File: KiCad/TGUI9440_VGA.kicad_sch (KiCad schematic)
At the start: 20 parts, among them U6 TGUI9440

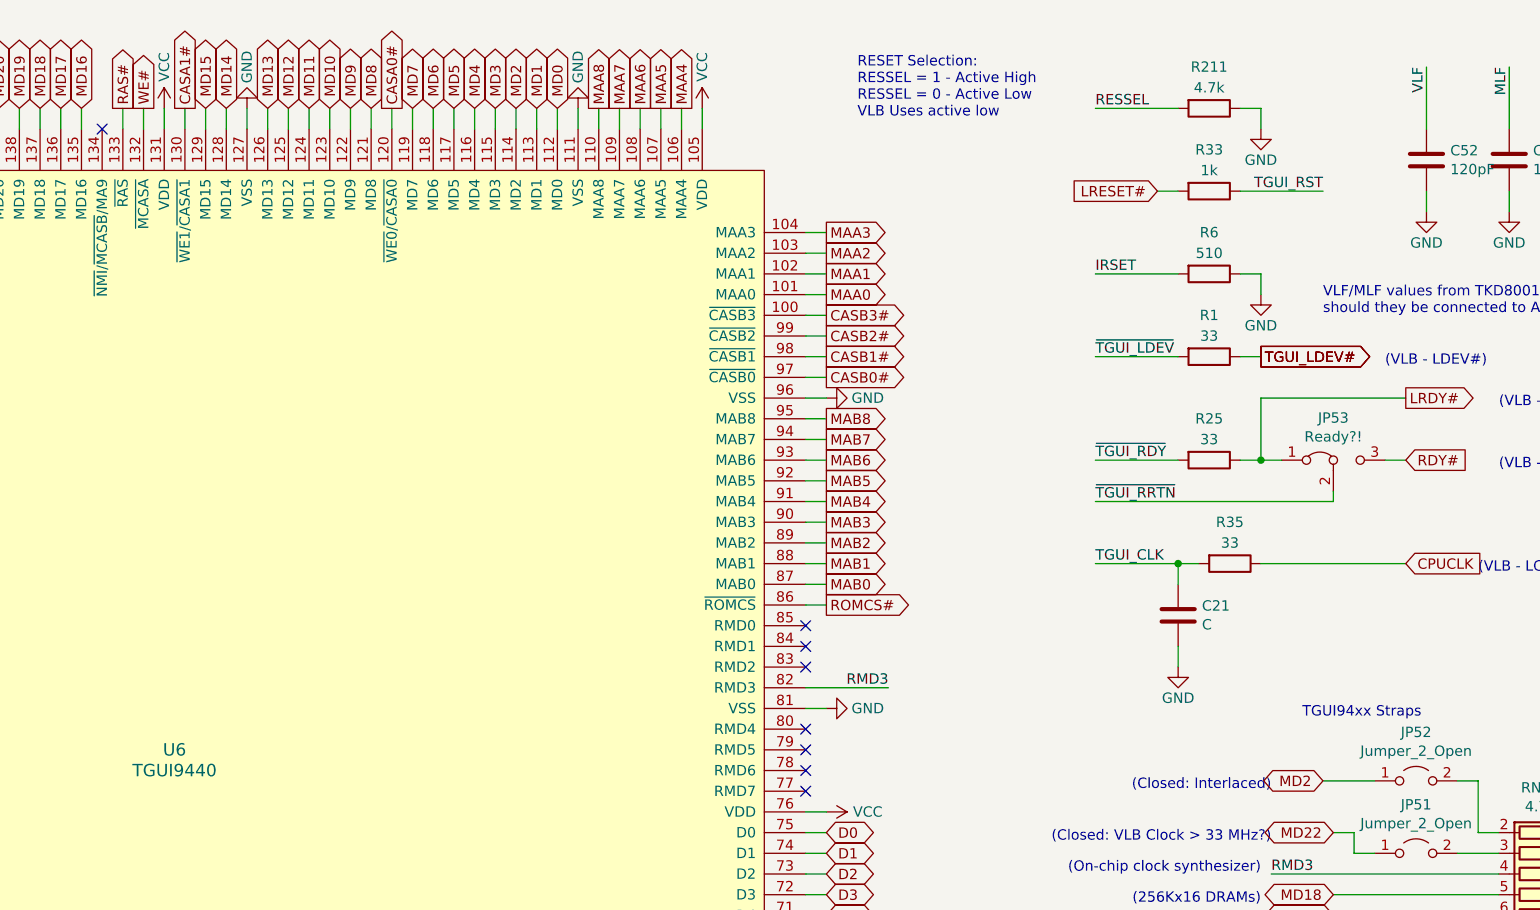
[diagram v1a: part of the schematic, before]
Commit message: Version 0.4: Update chipset connection
Signed-off-by: Sergey Kiselev <skiselev@gmail.com>
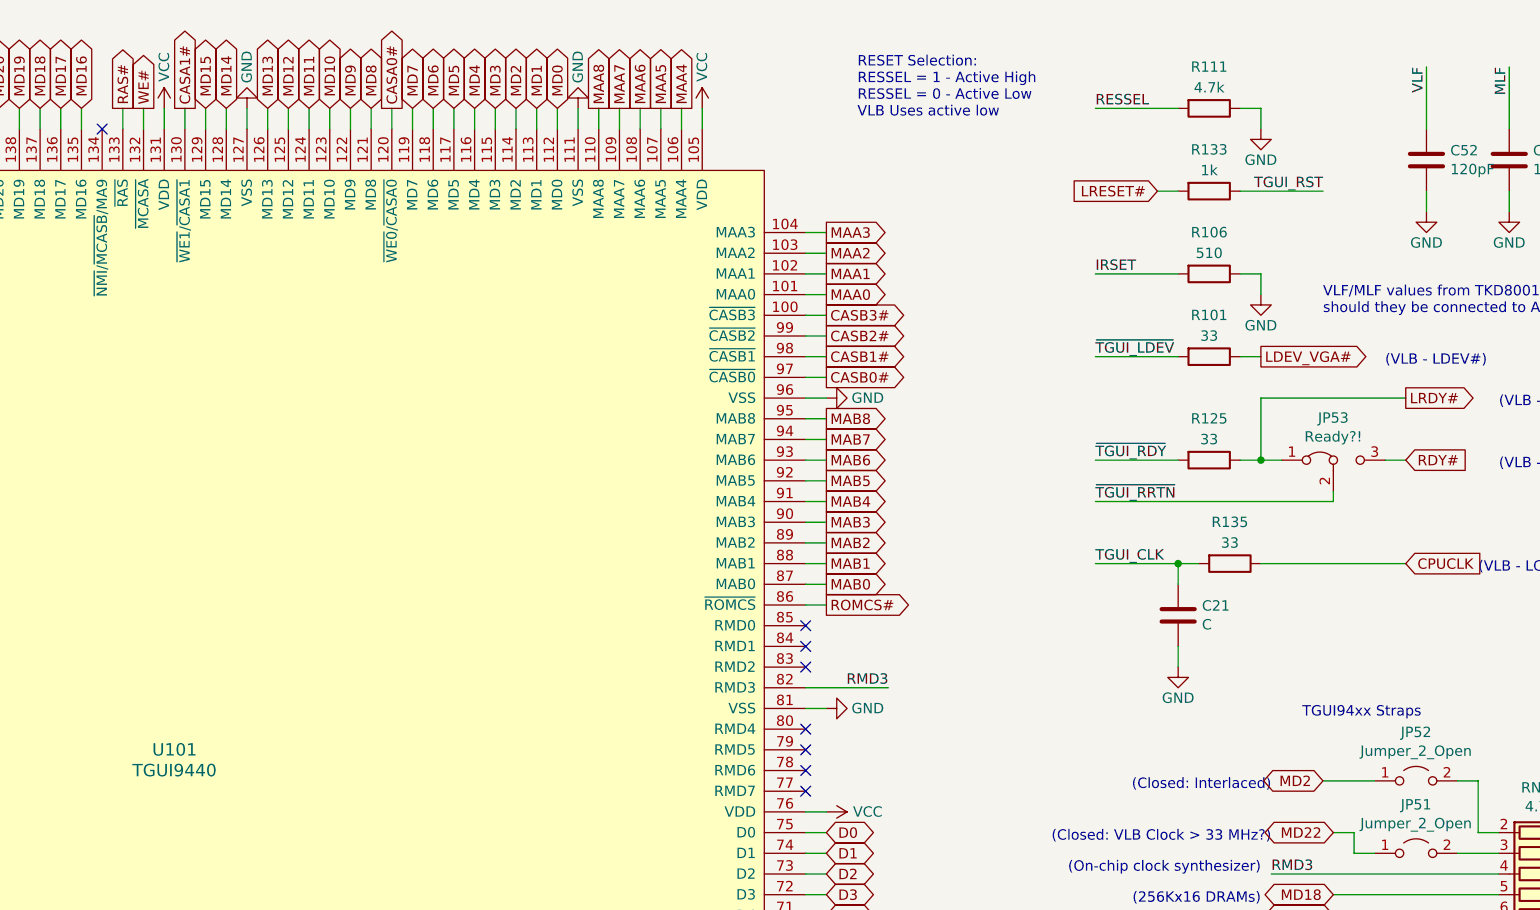
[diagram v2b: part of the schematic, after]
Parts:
- C20, C25, C26: footprint (none) -> Capacitor_THT:CP_Radial_D5.0mm_P2.00mm; symbol Device:CP1 -> Device:C_Polarized_US
- C21, C52, C53: footprint (none) -> Capacitor_SMD:C_0603_1608Metric_Pad1.08x0.95mm_HandSolder
- FB5: footprint (none) -> Inductor_SMD:L_0603_1608Metric_Pad1.05x0.95mm_HandSolder; symbol Device:Ferrite_Bead_Small -> Device:FerriteBead_Small
- JP51, JP52: footprint (none) -> My_Components:Conn_Pin_Header_2x1_2.54mm
- JP53: footprint (none) -> My_Components:Conn_Pin_Header_3x1_2.54mm
- L1, L2: footprint (none) -> Inductor_SMD:L_0603_1608Metric_Pad1.05x0.95mm_HandSolder
- R101: renamed from R1; footprint (none) -> Resistor_SMD:R_0612_1632Metric_Pad1.18x3.40mm_HandSolder
- R106: renamed from R6; footprint (none) -> Resistor_SMD:R_0612_1632Metric_Pad1.18x3.40mm_HandSolder
- R111: renamed from R211; footprint (none) -> Resistor_SMD:R_0612_1632Metric_Pad1.18x3.40mm_HandSolder
- R125: renamed from R25; footprint (none) -> Resistor_SMD:R_0612_1632Metric_Pad1.18x3.40mm_HandSolder
- R133: renamed from R33; footprint (none) -> Resistor_SMD:R_0612_1632Metric_Pad1.18x3.40mm_HandSolder
- R135: renamed from R35; footprint (none) -> Resistor_SMD:R_0612_1632Metric_Pad1.18x3.40mm_HandSolder
- U101: renamed from U6; footprint (none) -> Package_QFP:PQFP-208_28x28mm_P0.5mm
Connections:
- net TGUI_LDEV# renamed LDEV_VGA#
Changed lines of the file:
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@@
     )
   )
-  (global_label "TGUI_LDEV#" (shape output) (at 236.22 50.8 0) (fields_autoplaced)
-    (effects (font (size 1.27 1.27)) (justify left))
-    (property "Intersheet References" "${INTERSHEET_REFS}" (id 0) (at 0 0 0)
-      (effects (font (size 1.27 1.27)) hide)
+  (global_label "LDEV_VGA#" (shape output) (at 236.22 50.8 0) (fields_autoplaced)
+    (effects (font (size 1.27 1.27)) (justify left))
+    (property "Intersheet References" "${INTERSHEET_REFS}" (id 0) (at 248.7647 50.7206 0)
+      (effects (font (size 1.27 1.27)) (justify left) hide)
     )
   )
@@
   (global_label "ADS#" (shape input) (at 22.86 142.24 180) (fields_autoplaced)
     (effects (font (size 1.27 1.27)) (justify right))
-    (property "Intersheet References" "${INTERSHEET_REFS}" (id 0) (at 0 0 0)
-      (effects (font (size 1.27 1.27)) hide)
-    )
-  )
-  (global_label "TGUI_LDEV#" (shape output) (at 236.22 50.8 0) (fields_autoplaced)
-    (effects (font (size 1.27 1.27)) (justify left))
     (property "Intersheet References" "${INTERSHEET_REFS}" (id 0) (at 0 0 0)
       (effects (font (size 1.27 1.27)) hide)
@@
   (symbol (lib_id "my_components:TGUI9440") (at 102.87 100.33 0) (unit 1)
     (in_bom yes) (on_board yes)
-    (property "Reference" "U6" (id 0) (at 102.87 99.06 0)
+    (property "Reference" "U101" (id 0) (at 102.87 99.06 0)
       (effects (font (size 1.524 1.524)))
     )
@@
       (effects (font (size 1.524 1.524)))
     )
-    (property "Footprint" "" (id 2) (at 87.63 115.57 0)
+    (property "Footprint" "Package_QFP:PQFP-208_28x28mm_P0.5mm" (id 2) (at 87.63 115.57 0)
       (effects (font (size 1.524 1.524)) hide)
     )
@@
   (symbol (lib_id "Device:R") (at 229.87 20.32 270) (unit 1)
     (in_bom yes) (on_board yes)
-    (property "Reference" "R211" (id 0) (at 229.87 15.24 90))
+    (property "Reference" "R111" (id 0) (at 229.87 15.24 90))
     (property "Value" "4.7k" (id 1) (at 229.87 17.78 90))
-    (property "Footprint" "" (id 2) (at 229.87 18.542 90)
+    (property "Footprint" "Resistor_SMD:R_0612_1632Metric_Pad1.18x3.40mm_HandSolder" (id 2) (at 229.87 18.542 90)
       (effects (font (size 1.27 1.27)) hide)
     )
@@
   (symbol (lib_id "Device:R") (at 229.87 30.48 270) (unit 1)
     (in_bom yes) (on_board yes)
-    (property "Reference" "R33" (id 0) (at 229.87 25.4 90))
+    (property "Reference" "R133" (id 0) (at 229.87 25.4 90))
     (property "Value" "1k" (id 1) (at 229.87 27.94 90))
-    (property "Footprint" "" (id 2) (at 229.87 28.702 90)
+    (property "Footprint" "Resistor_SMD:R_0612_1632Metric_Pad1.18x3.40mm_HandSolder" (id 2) (at 229.87 28.702 90)
       (effects (font (size 1.27 1.27)) hide)
     )
@@
       (effects (font (size 1.27 1.27)) (justify left))
     )
-    (property "Footprint" "" (id 2) (at 257.5052 30.48 0)
+    (property "Footprint" "Capacitor_SMD:C_0603_1608Metric_Pad1.08x0.95mm_HandSolder" (id 2) (at 257.5052 30.48 0)
       (effects (font (size 1.27 1.27)) hide)
     )
@@
       (effects (font (size 1.27 1.27)) (justify left))
     )
-    (property "Footprint" "" (id 2) (at 267.6652 30.48 0)
+    (property "Footprint" "Capacitor_SMD:C_0603_1608Metric_Pad1.08x0.95mm_HandSolder" (id 2) (at 267.6652 30.48 0)
       (effects (font (size 1.27 1.27)) hide)
     )
@@
   (symbol (lib_id "Device:R") (at 229.87 40.64 270) (unit 1)
     (in_bom yes) (on_board yes)
-    (property "Reference" "R6" (id 0) (at 229.87 35.56 90))
+    (property "Reference" "R106" (id 0) (at 229.87 35.56 90))
     (property "Value" "510" (id 1) (at 229.87 38.1 90))
-    (property "Footprint" "" (id 2) (at 229.87 38.862 90)
+    (property "Footprint" "Resistor_SMD:R_0612_1632Metric_Pad1.18x3.40mm_HandSolder" (id 2) (at 229.87 38.862 90)
       (effects (font (size 1.27 1.27)) hide)
     )
@@
     (property "Reference" "JP52" (id 0) (at 255.27 96.901 0))
     (property "Value" "Jumper_2_Open" (id 1) (at 255.27 99.2124 0))
-    (property "Footprint" "" (id 2) (at 255.27 102.87 0)
+    (property "Footprint" "My_Components:Conn_Pin_Header_2x1_2.54mm" (id 2) (at 255.27 102.87 0)
       (effects (font (size 1.27 1.27)) hide)
     )
@@
     (property "Reference" "JP51" (id 0) (at 255.27 105.791 0))
     (property "Value" "Jumper_2_Open" (id 1) (at 255.27 108.1024 0))
-    (property "Footprint" "" (id 2) (at 255.27 111.76 0)
+    (property "Footprint" "My_Components:Conn_Pin_Header_2x1_2.54mm" (id 2) (at 255.27 111.76 0)
       (effects (font (size 1.27 1.27)) hide)
     )
@@
     (pin "2")
   )
-  (symbol (lib_id "Device:Ferrite_Bead_Small") (at 255.27 157.48 270) (unit 1)
+  (symbol (lib_id "Device:FerriteBead_Small") (at 255.27 157.48 270) (unit 1)
     (in_bom yes) (on_board yes)
     (property "Reference" "FB5" (id 0) (at 255.27 151.4602 90))
     (property "Value" "Ferrite_Bead" (id 1) (at 255.27 153.7716 90))
-    (property "Footprint" "" (id 2) (at 255.27 155.702 90)
+    (property "Footprint" "Inductor_SMD:L_0603_1608Metric_Pad1.05x0.95mm_HandSolder" (id 2) (at 255.27 155.702 90)
       (effects (font (size 1.27 1.27)) hide)
     )
@@
     (property "Reference" "L1" (id 0) (at 256.54 139.954 90))
     (property "Value" "2.7uH" (id 1) (at 256.54 142.2654 90))
-    (property "Footprint" "" (id 2) (at 256.54 144.78 0)
+    (property "Footprint" "Inductor_SMD:L_0603_1608Metric_Pad1.05x0.95mm_HandSolder" (id 2) (at 256.54 144.78 0)
       (effects (font (size 1.27 1.27)) hide)
     )
@@
     (pin "2")
   )
-  (symbol (lib_id "Device:CP1") (at 265.43 151.13 0) (unit 1)
+  (symbol (lib_id "Device:C_Polarized_US") (at 265.43 151.13 0) (unit 1)
     (in_bom yes) (on_board yes)
     (property "Reference" "C25" (id 0) (at 268.351 149.9616 0)
@@
       (effects (font (size 1.27 1.27)) (justify left))
     )
-    (property "Footprint" "" (id 2) (at 265.43 151.13 0)
+    (property "Footprint" "Capacitor_THT:CP_Radial_D5.0mm_P2.00mm" (id 2) (at 265.43 151.13 0)
       (effects (font (size 1.27 1.27)) hide)
     )
@@
     (property "Reference" "L2" (id 0) (at 233.68 139.954 90))
     (property "Value" "2.7uH" (id 1) (at 233.68 142.2654 90))
-    (property "Footprint" "" (id 2) (at 233.68 144.78 0)
+    (property "Footprint" "Inductor_SMD:L_0603_1608Metric_Pad1.05x0.95mm_HandSolder" (id 2) (at 233.68 144.78 0)
       (effects (font (size 1.27 1.27)) hide)
     )
@@
     (pin "2")
   )
-  (symbol (lib_id "Device:CP1") (at 224.79 151.13 0) (unit 1)
+  (symbol (lib_id "Device:C_Polarized_US") (at 224.79 151.13 0) (unit 1)
     (in_bom yes) (on_board yes)
     (property "Reference" "C26" (id 0) (at 227.711 149.9616 0)
@@
       (effects (font (size 1.27 1.27)) (justify left))
     )
-    (property "Footprint" "" (id 2) (at 224.79 151.13 0)
+    (property "Footprint" "Capacitor_THT:CP_Radial_D5.0mm_P2.00mm" (id 2) (at 224.79 151.13 0)
       (effects (font (size 1.27 1.27)) hide)
     )
@@
     (pin "2")
   )
-  (symbol (lib_id "Device:CP1") (at 245.11 151.13 0) (unit 1)
+  (symbol (lib_id "Device:C_Polarized_US") (at 245.11 151.13 0) (unit 1)
     (in_bom yes) (on_board yes)
     (property "Reference" "C20" (id 0) (at 248.031 149.9616 0)
@@
       (effects (font (size 1.27 1.27)) (justify left))
     )
-    (property "Footprint" "" (id 2) (at 245.11 151.13 0)
+    (property "Footprint" "Capacitor_THT:CP_Radial_D5.0mm_P2.00mm" (id 2) (at 245.11 151.13 0)
       (effects (font (size 1.27 1.27)) hide)
     )
@@
   (symbol (lib_id "Device:R") (at 229.87 50.8 270) (unit 1)
     (in_bom yes) (on_board yes)
-    (property "Reference" "R1" (id 0) (at 229.87 45.72 90))
+    (property "Reference" "R101" (id 0) (at 229.87 45.72 90))
     (property "Value" "33" (id 1) (at 229.87 48.26 90))
-    (property "Footprint" "" (id 2) (at 229.87 49.022 90)
+    (property "Footprint" "Resistor_SMD:R_0612_1632Metric_Pad1.18x3.40mm_HandSolder" (id 2) (at 229.87 49.022 90)
       (effects (font (size 1.27 1.27)) hide)
     )
@@
   (symbol (lib_id "Device:R") (at 229.87 63.5 270) (unit 1)
     (in_bom yes) (on_board yes)
-    (property "Reference" "R25" (id 0) (at 229.87 58.42 90))
+    (property "Reference" "R125" (id 0) (at 229.87 58.42 90))
     (property "Value" "33" (id 1) (at 229.87 60.96 90))
-    (property "Footprint" "" (id 2) (at 229.87 61.722 90)
+    (property "Footprint" "Resistor_SMD:R_0612_1632Metric_Pad1.18x3.40mm_HandSolder" (id 2) (at 229.87 61.722 90)
       (effects (font (size 1.27 1.27)) hide)
     )
@@
     (property "Reference" "JP53" (id 0) (at 245.11 58.3184 0))
     (property "Value" "Ready?!" (id 1) (at 245.11 60.6298 0))
-    (property "Footprint" "" (id 2) (at 245.11 63.5 0)
+    (property "Footprint" "My_Components:Conn_Pin_Header_3x1_2.54mm" (id 2) (at 245.11 63.5 0)
       (effects (font (size 1.27 1.27)) hide)
     )
@@
   (symbol (lib_id "Device:R") (at 232.41 76.2 270) (unit 1)
     (in_bom yes) (on_board yes)
-    (property "Reference" "R35" (id 0) (at 232.41 71.12 90))
+    (property "Reference" "R135" (id 0) (at 232.41 71.12 90))
     (property "Value" "33" (id 1) (at 232.41 73.66 90))
-    (property "Footprint" "" (id 2) (at 232.41 74.422 90)
+    (property "Footprint" "Resistor_SMD:R_0612_1632Metric_Pad1.18x3.40mm_HandSolder" (id 2) (at 232.41 74.422 90)
       (effects (font (size 1.27 1.27)) hide)
     )
@@
       (effects (font (size 1.27 1.27)) (justify left))
     )
-    (property "Footprint" "" (id 2) (at 227.0252 86.36 0)
-      (effects (font (size 1.27 1.27)) hide)
-    )
+    (property "Footprint" "Capacitor_SMD:C_0603_1608Metric_Pad1.08x0.95mm_HandSolder" (id 2) (at 227.0252 86.36 0)
+      (effects (font (size 1.27 1.27)) hide)
+    )

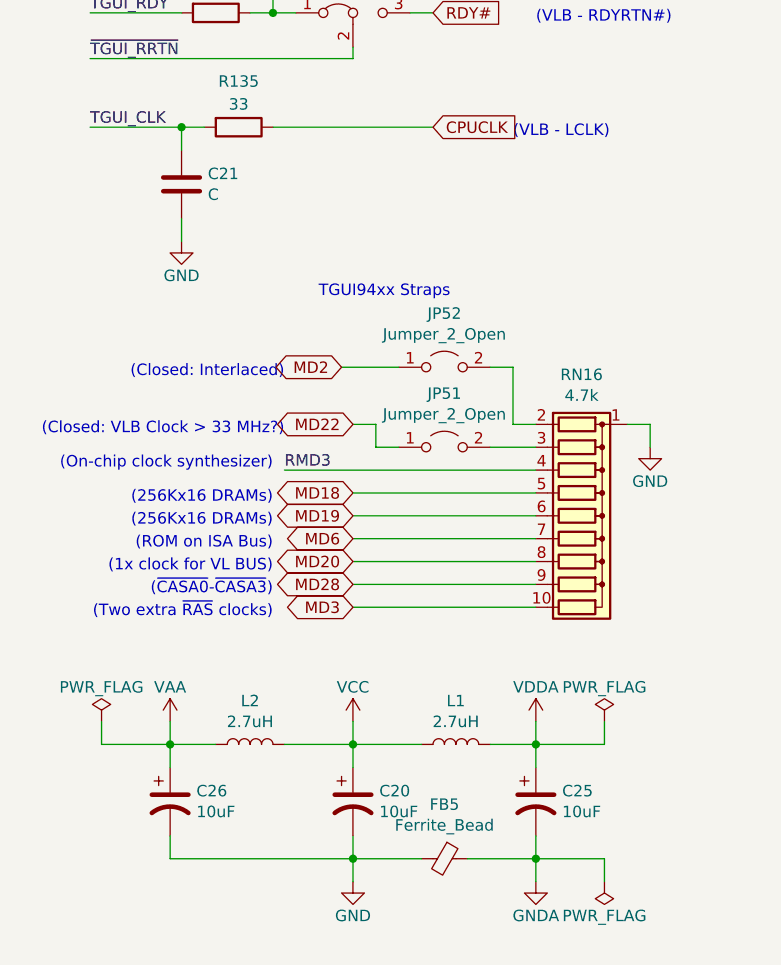
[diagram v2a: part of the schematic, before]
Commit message: More schematic updates. Remove old KiCad files
Signed-off-by: Sergey Kiselev <skiselev@gmail.com>
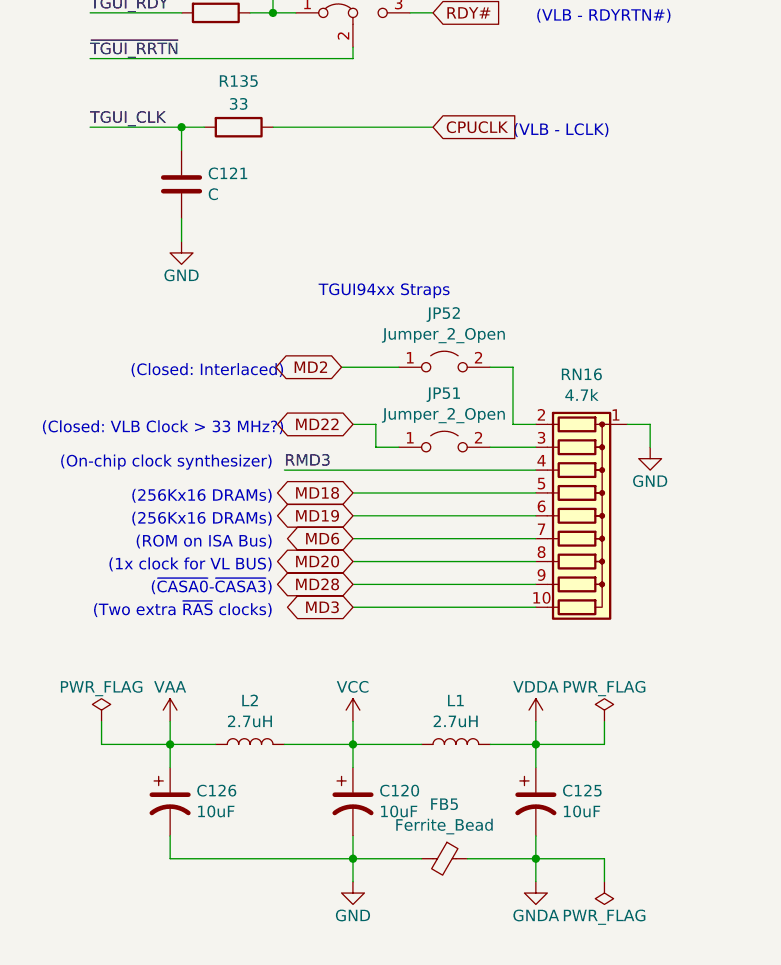
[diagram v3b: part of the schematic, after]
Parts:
- renumbered C20 to C120, C21 to C121, C25 to C125, C26 to C126
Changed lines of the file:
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@@
   (symbol (lib_id "Device:C_Polarized_US") (at 265.43 151.13 0) (unit 1)
     (in_bom yes) (on_board yes)
-    (property "Reference" "C25" (id 0) (at 268.351 149.9616 0)
+    (property "Reference" "C125" (id 0) (at 268.351 149.9616 0)
       (effects (font (size 1.27 1.27)) (justify left))
     )
@@
   (symbol (lib_id "Device:C_Polarized_US") (at 224.79 151.13 0) (unit 1)
     (in_bom yes) (on_board yes)
-    (property "Reference" "C26" (id 0) (at 227.711 149.9616 0)
+    (property "Reference" "C126" (id 0) (at 227.711 149.9616 0)
       (effects (font (size 1.27 1.27)) (justify left))
     )
@@
   (symbol (lib_id "Device:C_Polarized_US") (at 245.11 151.13 0) (unit 1)
     (in_bom yes) (on_board yes)
-    (property "Reference" "C20" (id 0) (at 248.031 149.9616 0)
+    (property "Reference" "C120" (id 0) (at 248.031 149.9616 0)
       (effects (font (size 1.27 1.27)) (justify left))
     )
@@
   (symbol (lib_id "Device:C") (at 226.06 82.55 0) (unit 1)
     (in_bom yes) (on_board yes)
-    (property "Reference" "C21" (id 0) (at 228.981 81.3816 0)
-      (effects (font (size 1.27 1.27)) (justify left))
-    )
+    (property "Reference" "C121" (id 0) (at 228.981 81.3816 0)
+      (effects (font (size 1.27 1.27)) (justify left))
+    )
